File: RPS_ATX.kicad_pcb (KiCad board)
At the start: 2 copper layers, 100 x 50 mm, 73 parts, among them J1 Fan_in, J10 CTRL, J13 Fan_out, J2 494_OUT, J3 POT, J4 17.5V, J5 PS_OUT-, J6 PS_OUT+, J7 RPS_OUT-, J8 MEAS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

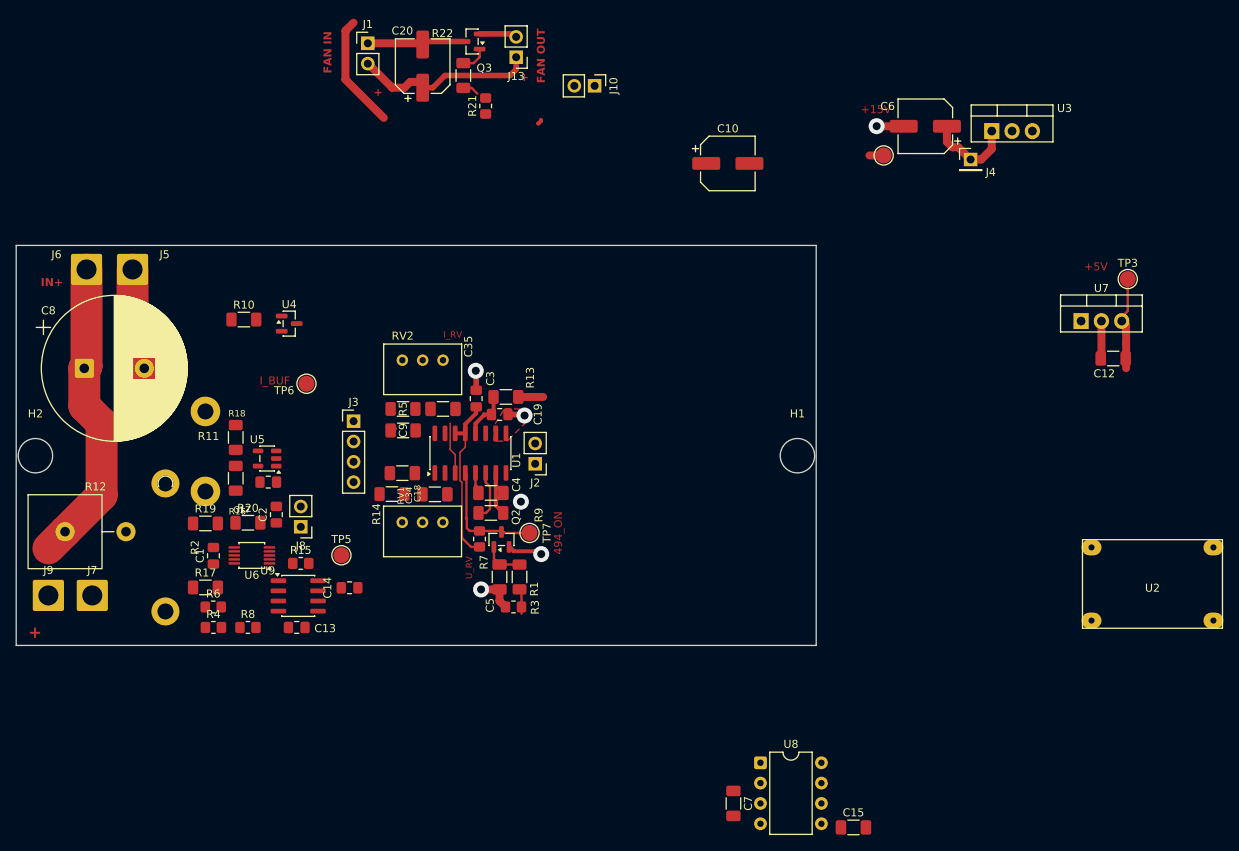
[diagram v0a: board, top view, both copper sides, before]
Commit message: lm358 as U and I meas
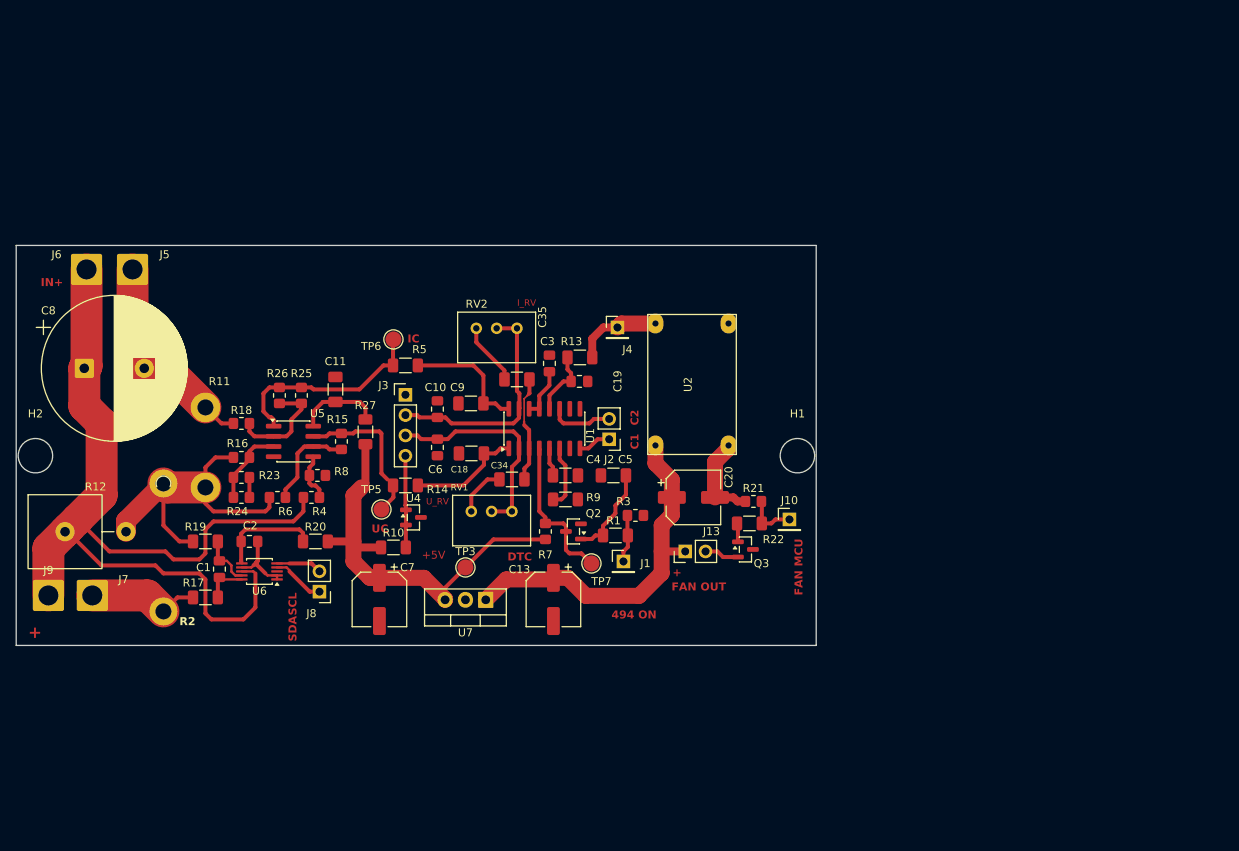
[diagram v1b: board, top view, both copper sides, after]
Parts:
- removed C12, C15: 10u, Capacitor_SMD:C_1206_3216Metric_Pad1.33x1.80mm_HandSolder
- removed C14, C17: 100n, Capacitor_SMD:C_0805_2012Metric_Pad1.18x1.45mm_HandSolder
- removed TP2: +15V, TestPoint:TestPoint_Pad_D2.0mm
- removed U3: L7815, Package_TO_SOT_THT:TO-220-3_Vertical
- removed U8: ICL7660, Package_DIP:DIP-8_W7.62mm
- removed U9: OP07, Package_SO:SOIC-8_3.9x4.9mm_P1.27mm
- added C11: 10u, Capacitor_SMD:C_1206_3216Metric_Pad1.33x1.80mm_HandSolder, F.Cu at (94.2, 73.2)
- added R23: 10K 0.01%, Resistor_SMD:R_0805_2012Metric_Pad1.20x1.40mm_HandSolder, F.Cu at (82.5, 84.2)
- added R24: 10K 0.01%, Resistor_SMD:R_0805_2012Metric_Pad1.20x1.40mm_HandSolder, F.Cu at (82.5, 86.8)
- added R25: 10K 0.01%, Resistor_SMD:R_0805_2012Metric_Pad1.20x1.40mm_HandSolder, F.Cu at (90.0, 74.0)
- added R26: 10K 0.01%, Resistor_SMD:R_0805_2012Metric_Pad1.20x1.40mm_HandSolder, F.Cu at (87.2, 74.0)
- added R27: 10R, Resistor_SMD:R_1206_3216Metric_Pad1.30x1.75mm_HandSolder, F.Cu at (98.0, 78.5)
- C10, C6: value 100uF -> 100n; footprint Capacitor_SMD:CP_Elec_6.3x5.4_Nichicon -> Capacitor_SMD:C_0805_2012Metric_Pad1.18x1.45mm_HandSolder
- C13: value 100n -> 100uF; footprint Capacitor_SMD:C_0805_2012Metric_Pad1.18x1.45mm_HandSolder -> Capacitor_SMD:CP_Elec_6.3x5.4_Nichicon
- C7: value 10u -> 100uF; footprint Capacitor_SMD:C_1206_3216Metric_Pad1.33x1.80mm_HandSolder -> Capacitor_SMD:CP_Elec_6.3x5.4_Nichicon
- J1: value Fan_in -> 494_ON; footprint Connector_PinHeader_2.54mm:PinHeader_1x02_P2.54mm_Vertical -> Connector_PinHeader_2.54mm:PinHeader_1x01_P2.54mm_Vertical
- J10: value CTRL -> MCU_FAN; footprint Connector_PinHeader_2.54mm:PinHeader_1x02_P2.54mm_Vertical -> Connector_PinHeader_2.54mm:PinHeader_1x01_P2.54mm_Vertical
- R16, R18: value 10R -> 1K 0.01%; footprint Resistor_SMD:R_1206_3216Metric_Pad1.30x1.75mm_HandSolder -> Resistor_SMD:R_0805_2012Metric_Pad1.20x1.40mm_HandSolder
- U5: value INA180A2 -> LM358; footprint Package_TO_SOT_SMD:SOT-23-5 -> Package_SO:SOIC-8_3.9x4.9mm_P1.27mm
- moved TP3 90.3 mm to (110.5, 95.5)
- moved U7 82.2 mm to (113.0, 99.5), turned to 180 degrees
- moved C6 73.0 mm to (107.0, 80.5), turned to -90 degrees
- moved J1 72.2 mm to (130.2, 94.8)
- moved Q3 72.1 mm to (145.5, 93.2), turned to 0 degrees
- moved R22 66.4 mm to (146.0, 90.0), turned to 180 degrees
- moved J13 65.3 mm to (138.0, 93.5), turned to 90 degrees
- moved C20 63.7 mm to (139.0, 86.8), turned to 0 degrees
- moved U2 62.7 mm to (138.8, 72.6), turned to -90 degrees
- moved R21 59.7 mm to (146.5, 87.2), turned to 0 degrees
- moved J10 59.4 mm to (151.0, 89.5), turned to 0 degrees
- moved C7 51.1 mm to (99.8, 99.5)
- moved J4 48.9 mm to (129.5, 65.5)
- moved C10 47.5 mm to (107.0, 75.7), turned to 90 degrees
- moved R10 34.1 mm to (101.5, 93.0)
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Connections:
- C10 pad 1: +15V -> I_2IN-
- C13 pad 1: -5V -> +8V
- C2 pad 1: +5V -> Net-(U6-VS)
- C20 pad 1: /fan+ -> +8V
- C20 pad 2: Net-(J1-Pin_1) -> GND
- C6 pad 1: +17.5V_ATX -> U_1IN-
- C7 pad 1: Net-(U8-CAP+) -> +5V
- C7 pad 2: Net-(U8-CAP-) -> GND
- J1 pad 1: Net-(J1-Pin_1) -> MCU_494_ON
- J10 pad 1: MCU_494_ON -> MCU_FAN
- J13 pad 1: /fan+ -> +8V
- Q3 pad 3: Net-(J1-Pin_1) -> GND
- R10 pad 1: +5V_REF -> +5V
- R15 pad 1: Net-(U9--) -> Net-(U5B--)
- R16 pad 1: MEAS_I+ -> /Analog/sh_meas_r+
- R16 pad 2: /Analog/sh_meas_r+ -> MEAS_I+
- R4 pad 2: Net-(U9-+) -> Net-(U5B-+)
- R6 pad 2: Net-(U9--) -> Net-(U5B--)
- R7 pad 1: +5V_REF -> +5V
- R8 pad 1: Net-(U9-+) -> Net-(U5B-+)
- U5 pad 2: GND -> /Analog/sh_meas_r-
- U5 pad 4: /Analog/sh_meas_r- -> GND
- U5 pad 5: +5V -> Net-(U5B-+)
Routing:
- net VOUT: track 38.6 -> 118.4 mm
- net +8V: track 0.32 -> 45.5 mm
- net MEAS_I+: track 0.65 -> 42.2 mm
- net +5V: track 12.0 -> 52.3 mm
- net I_2IN-: track 0.14 -> 29.0 mm
- net U_1IN-: track 0.00 -> 27.3 mm
- net /Analog/i_op_out: track 0.49 -> 25.9 mm
- net /fan+: track 22.6 -> 0.00 mm
- net Net-(R14-Pad1): track 0.00 -> 18.6 mm
- net +15V: track 16.6 -> 0.00 mm
- net I_2IN+: track 0.09 -> 15.7 mm
- net +5V_REF: track 21.2 -> 6.43 mm
- net Net-(J7-Pin_1): track 0.00 -> 14.1 mm
- net U_1IN+: track 0.00 -> 14.1 mm
- net /Analog/sh_meas_r-: track 0.00 -> 13.5 mm
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- removed copper zone on F.Cu, net GND
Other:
- board text added: "494 ON"
- board text added: "C1"
- board text added: "C2"
- board text added: "DTC"
- board text added: "FAN MCU"
- board text added: "IC"
- board text added: "SCL"
- board text added: "SDA"
- board text added: "UC"
- board text removed: "FAN IN"

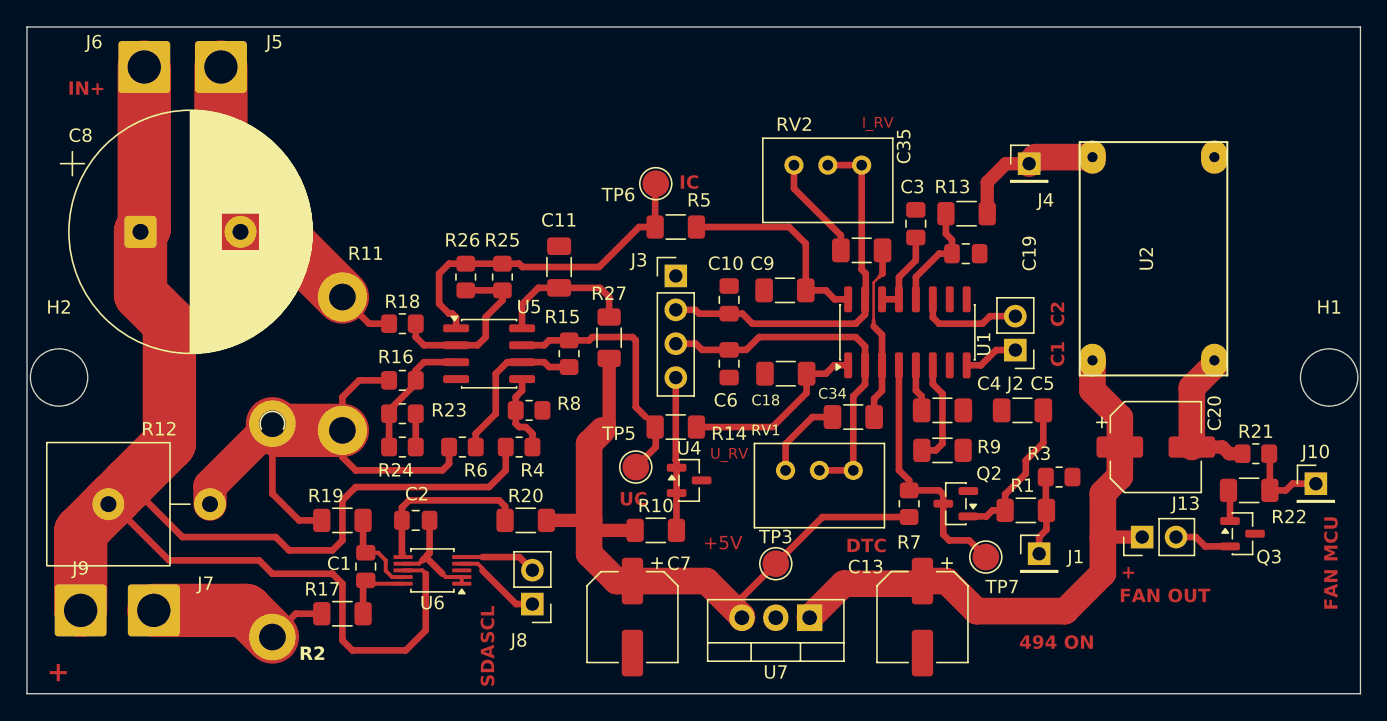
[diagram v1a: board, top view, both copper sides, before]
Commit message: added gnd vias, need to isolate power and signal GND
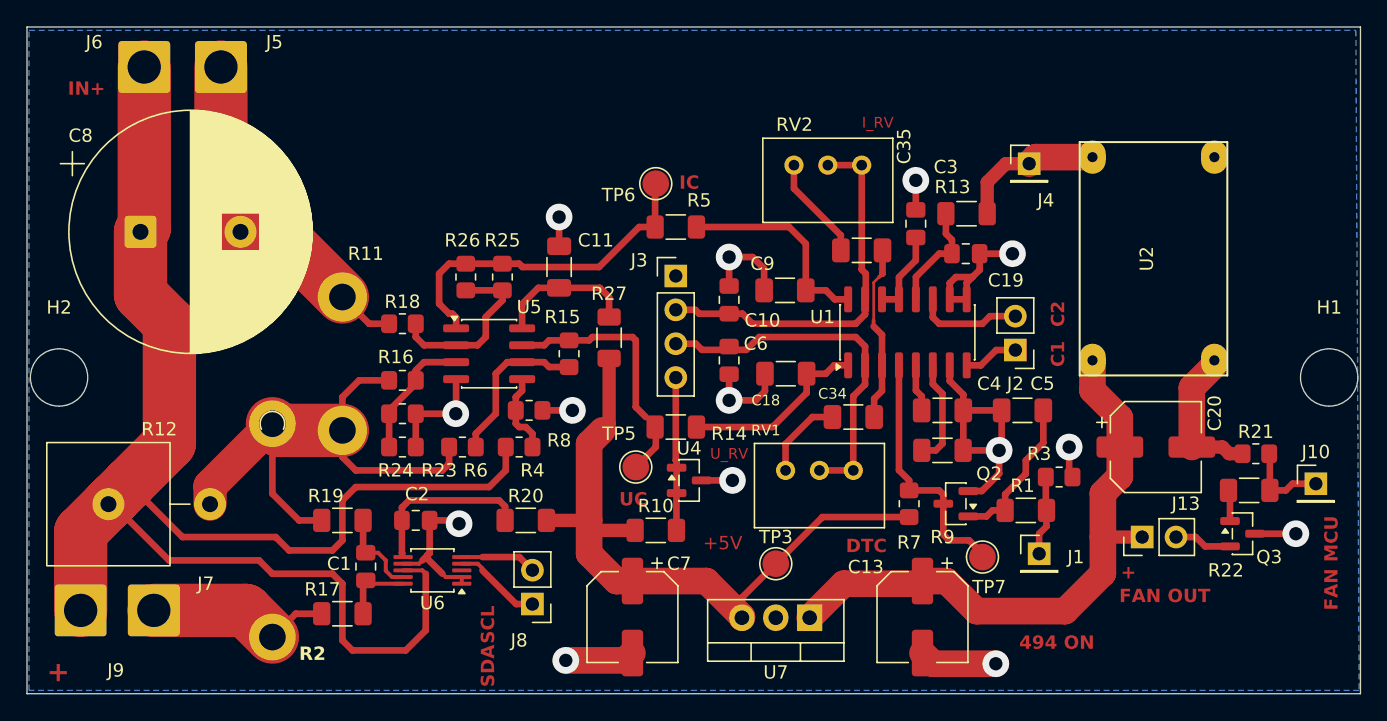
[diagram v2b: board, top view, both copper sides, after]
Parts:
- moved C6 0.25 mm to (107.0, 80.2)
- moved TP7 0.25 mm to (126.0, 95.0), turned to 0 degrees
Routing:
- net GND: track 49.3 -> 126.4 mm, vias 0 -> 14
- added copper zone on B.Cu, net GND

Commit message: kind of ready
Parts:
- removed J4: 17.5V, Connector_PinHeader_2.54mm:PinHeader_1x01_P2.54mm_Vertical
- added J11: PW_IN, Connector_PinHeader_2.54mm:PinHeader_1x02_P2.54mm_Vertical, F.Cu at (129.5, 65.5)
- J13: value Fan_out -> FAN_OUT
